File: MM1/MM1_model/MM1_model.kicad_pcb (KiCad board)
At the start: 4 copper layers, 64 x 47 mm, 2 parts, among them J1 MM1_receptacle_5530843-2, J2 MM1_addressExtension

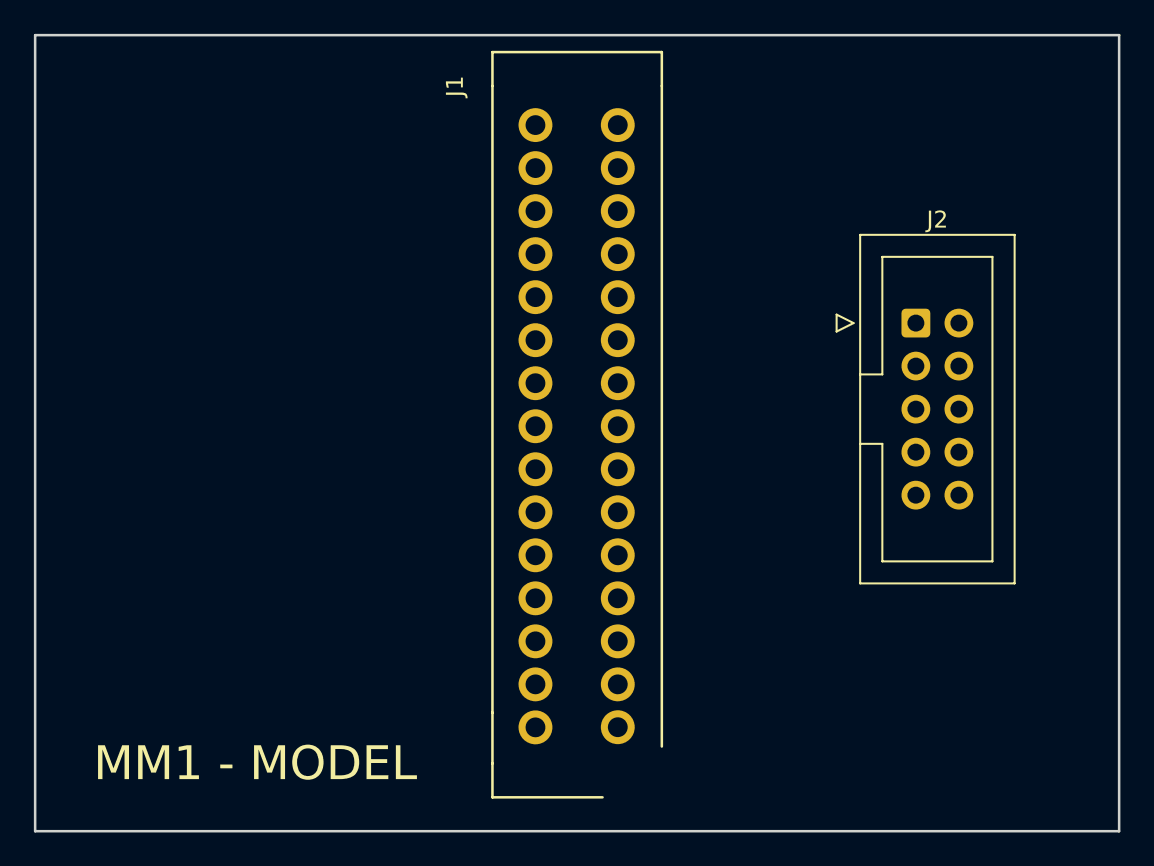
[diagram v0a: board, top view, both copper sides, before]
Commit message: Replacing "edge.cut" by "margin"
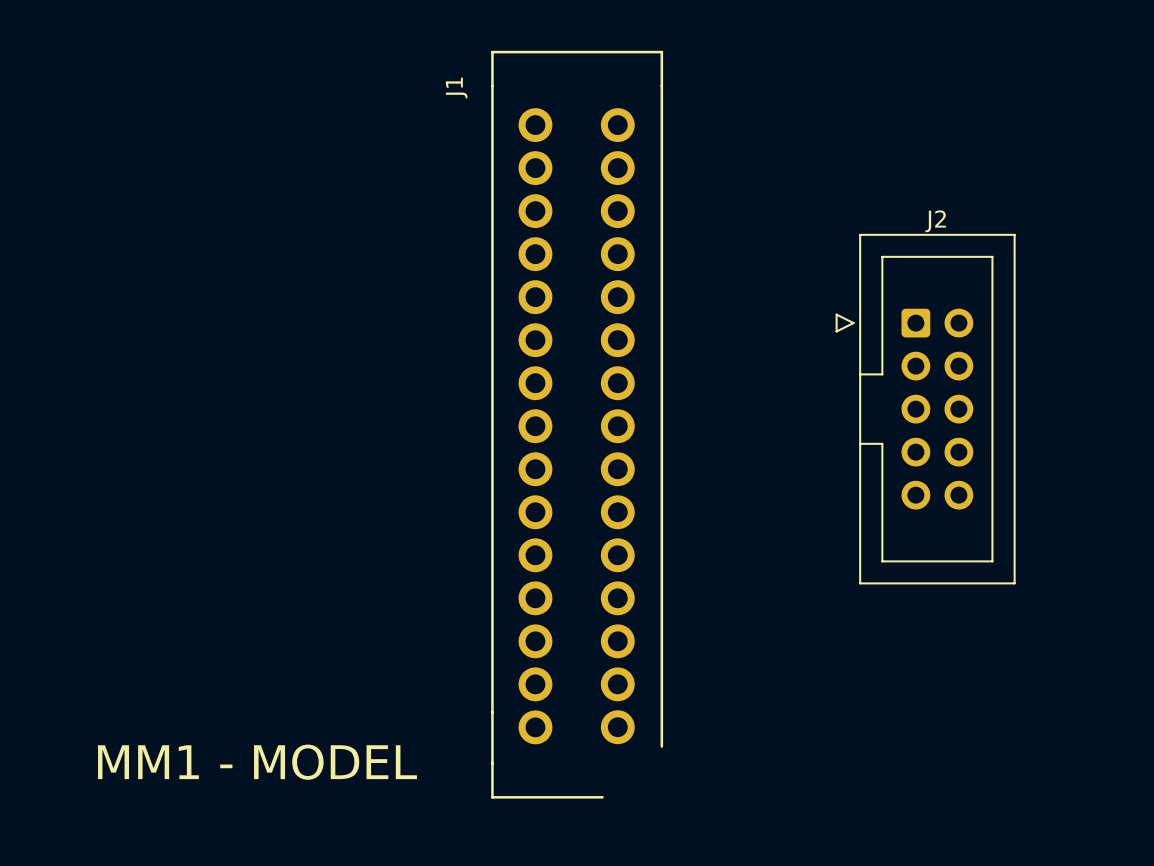
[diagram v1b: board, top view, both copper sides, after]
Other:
- board outline removed
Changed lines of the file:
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@@
       (effects (font (size 1 1) (thickness 0.15)))
     )
+    (fp_line (start 20 5) (end -19 5) (layer F.SilkS) (width 0.15))
+    (fp_line (start 22 -5) (end 20 -5) (layer F.SilkS) (width 0.15))
+    (fp_line (start 22 5) (end 22 -5) (layer F.SilkS) (width 0.15))
+    (fp_line (start 20 5) (end 22 5) (layer F.SilkS) (width 0.15))
+    (fp_line (start -22 -5) (end -20 -5) (layer F.SilkS) (width 0.15))
+    (fp_line (start -22 1.5) (end -22 -5) (layer F.SilkS) (width 0.15))
+    (fp_line (start -20 -5) (end -17 -5) (layer F.SilkS) (width 0.15))
     (fp_line (start -17 -5) (end 20 -5) (layer F.SilkS) (width 0.15))
-    (fp_line (start -20 -5) (end -17 -5) (layer F.SilkS) (width 0.15))
-    (fp_line (start -22 1.5) (end -22 -5) (layer F.SilkS) (width 0.15))
-    (fp_line (start -22 -5) (end -20 -5) (layer F.SilkS) (width 0.15))
-    (fp_line (start 20 5) (end 22 5) (layer F.SilkS) (width 0.15))
-    (fp_line (start 22 5) (end 22 -5) (layer F.SilkS) (width 0.15))
-    (fp_line (start 22 -5) (end 20 -5) (layer F.SilkS) (width 0.15))
-    (fp_line (start 20 5) (end -19 5) (layer F.SilkS) (width 0.15))
     (pad 2 thru_hole circle (at -17.87 -2.46 90) (size 2 2) (drill 1.1684) (layers *.Cu *.Mask)
       (net 4 /MEMADDRESS_0))
@@
       (effects (font (size 1 1) (thickness 0.15)))
     )
+    (fp_line (start -3.18 -4.1) (end -2.18 -5.1) (layer F.Fab) (width 0.1))
+    (fp_line (start -2.18 -5.1) (end 5.72 -5.1) (layer F.Fab) (width 0.1))
+    (fp_line (start 5.72 -5.1) (end 5.72 15.26) (layer F.Fab) (width 0.1))
+    (fp_line (start 5.72 15.26) (end -3.18 15.26) (layer F.Fab) (width 0.1))
+    (fp_line (start -3.18 15.26) (end -3.18 -4.1) (layer F.Fab) (width 0.1))
+    (fp_line (start -3.18 3.03) (end -1.98 3.03) (layer F.Fab) (width 0.1))
+    (fp_line (start -1.98 3.03) (end -1.98 -3.91) (layer F.Fab) (width 0.1))
+    (fp_line (start -1.98 -3.91) (end 4.52 -3.91) (layer F.Fab) (width 0.1))
+    (fp_line (start 4.52 -3.91) (end 4.52 14.07) (layer F.Fab) (width 0.1))
+    (fp_line (start 4.52 14.07) (end -1.98 14.07) (layer F.Fab) (width 0.1))
+    (fp_line (start -1.98 14.07) (end -1.98 7.13) (layer F.Fab) (width 0.1))
+    (fp_line (start -1.98 7.13) (end -1.98 7.13) (layer F.Fab) (width 0.1))
+    (fp_line (start -1.98 7.13) (end -3.18 7.13) (layer F.Fab) (width 0.1))
+    (fp_line (start -3.29 -5.21) (end 5.83 -5.21) (layer F.SilkS) (width 0.12))
+    (fp_line (start 5.83 -5.21) (end 5.83 15.37) (layer F.SilkS) (width 0.12))
+    (fp_line (start 5.83 15.37) (end -3.29 15.37) (layer F.SilkS) (width 0.12))
+    (fp_line (start -3.29 15.37) (end -3.29 -5.21) (layer F.SilkS) (width 0.12))
+    (fp_line (start -3.29 3.03) (end -1.98 3.03) (layer F.SilkS) (width 0.12))
+    (fp_line (start -1.98 3.03) (end -1.98 -3.91) (layer F.SilkS) (width 0.12))
+    (fp_line (start -1.98 -3.91) (end 4.52 -3.91) (layer F.SilkS) (width 0.12))
+    (fp_line (start 4.52 -3.91) (end 4.52 14.07) (layer F.SilkS) (width 0.12))
+    (fp_line (start 4.52 14.07) (end -1.98 14.07) (layer F.SilkS) (width 0.12))
+    (fp_line (start -1.98 14.07) (end -1.98 7.13) (layer F.SilkS) (width 0.12))
+    (fp_line (start -1.98 7.13) (end -1.98 7.13) (layer F.SilkS) (width 0.12))
+    (fp_line (start -1.98 7.13) (end -3.29 7.13) (layer F.SilkS) (width 0.12))
+    (fp_line (start -3.68 0) (end -4.68 -0.5) (layer F.SilkS) (width 0.12))
+    (fp_line (start -4.68 -0.5) (end -4.68 0.5) (layer F.SilkS) (width 0.12))
+    (fp_line (start -4.68 0.5) (end -3.68 0) (layer F.SilkS) (width 0.12))
+    (fp_line (start -3.68 -5.6) (end -3.68 15.76) (layer F.CrtYd) (width 0.05))
+    (fp_line (start -3.68 15.76) (end 6.22 15.76) (layer F.CrtYd) (width 0.05))
+    (fp_line (start 6.22 15.76) (end 6.22 -5.6) (layer F.CrtYd) (width 0.05))
     (fp_line (start 6.22 -5.6) (end -3.68 -5.6) (layer F.CrtYd) (width 0.05))
-    (fp_line (start 6.22 15.76) (end 6.22 -5.6) (layer F.CrtYd) (width 0.05))
-    (fp_line (start -3.68 15.76) (end 6.22 15.76) (layer F.CrtYd) (width 0.05))
-    (fp_line (start -3.68 -5.6) (end -3.68 15.76) (layer F.CrtYd) (width 0.05))
-    (fp_line (start -4.68 0.5) (end -3.68 0) (layer F.SilkS) (width 0.12))
-    (fp_line (start -4.68 -0.5) (end -4.68 0.5) (layer F.SilkS) (width 0.12))
-    (fp_line (start -3.68 0) (end -4.68 -0.5) (layer F.SilkS) (width 0.12))
-    (fp_line (start -1.98 7.13) (end -3.29 7.13) (layer F.SilkS) (width 0.12))
-    (fp_line (start -1.98 7.13) (end -1.98 7.13) (layer F.SilkS) (width 0.12))
-    (fp_line (start -1.98 14.07) (end -1.98 7.13) (layer F.SilkS) (width 0.12))
-    (fp_line (start 4.52 14.07) (end -1.98 14.07) (layer F.SilkS) (width 0.12))
-    (fp_line (start 4.52 -3.91) (end 4.52 14.07) (layer F.SilkS) (width 0.12))
-    (fp_line (start -1.98 -3.91) (end 4.52 -3.91) (layer F.SilkS) (width 0.12))
-    (fp_line (start -1.98 3.03) (end -1.98 -3.91) (layer F.SilkS) (width 0.12))
-    (fp_line (start -3.29 3.03) (end -1.98 3.03) (layer F.SilkS) (width 0.12))
-    (fp_line (start -3.29 15.37) (end -3.29 -5.21) (layer F.SilkS) (width 0.12))
-    (fp_line (start 5.83 15.37) (end -3.29 15.37) (layer F.SilkS) (width 0.12))
-    (fp_line (start 5.83 -5.21) (end 5.83 15.37) (layer F.SilkS) (width 0.12))
-    (fp_line (start -3.29 -5.21) (end 5.83 -5.21) (layer F.SilkS) (width 0.12))
-    (fp_line (start -1.98 7.13) (end -3.18 7.13) (layer F.Fab) (width 0.1))
-    (fp_line (start -1.98 7.13) (end -1.98 7.13) (layer F.Fab) (width 0.1))
-    (fp_line (start -1.98 14.07) (end -1.98 7.13) (layer F.Fab) (width 0.1))
-    (fp_line (start 4.52 14.07) (end -1.98 14.07) (layer F.Fab) (width 0.1))
-    (fp_line (start 4.52 -3.91) (end 4.52 14.07) (layer F.Fab) (width 0.1))
-    (fp_line (start -1.98 -3.91) (end 4.52 -3.91) (layer F.Fab) (width 0.1))
-    (fp_line (start -1.98 3.03) (end -1.98 -3.91) (layer F.Fab) (width 0.1))
-    (fp_line (start -3.18 3.03) (end -1.98 3.03) (layer F.Fab) (width 0.1))
-    (fp_line (start -3.18 15.26) (end -3.18 -4.1) (layer F.Fab) (width 0.1))
-    (fp_line (start 5.72 15.26) (end -3.18 15.26) (layer F.Fab) (width 0.1))
-    (fp_line (start 5.72 -5.1) (end 5.72 15.26) (layer F.Fab) (width 0.1))
-    (fp_line (start -2.18 -5.1) (end 5.72 -5.1) (layer F.Fab) (width 0.1))
-    (fp_line (start -3.18 -4.1) (end -2.18 -5.1) (layer F.Fab) (width 0.1))
     (fp_text user %R (at 1.27 5.08 90) (layer F.Fab)
       (effects (font (size 1 1) (thickness 0.15)))
@@
     (effects (font (size 1 1) (thickness 0.15)))
   )
-  (gr_line (start 127 120) (end 127 73) (layer Edge.Cuts) (width 0.15))
-  (gr_line (start 191 120) (end 127 120) (layer Edge.Cuts) (width 0.15))
-  (gr_line (start 191 73) (end 191 120) (layer Edge.Cuts) (width 0.15))
-  (gr_line (start 127 73) (end 191 73) (layer Edge.Cuts) (width 0.15))
+  (gr_line (start 127 120) (end 127 73) (layer Margin) (width 0.15))
+  (gr_line (start 191 120) (end 127 120) (layer Margin) (width 0.15))
+  (gr_line (start 191 73) (end 191 120) (layer Margin) (width 0.15))
+  (gr_line (start 127 73) (end 191 73) (layer Margin) (width 0.15))
   (gr_text "MM1 - MODEL" (at 140 116) (layer F.SilkS)
     (effects (font (size 2 2) (thickness 0.5)))
